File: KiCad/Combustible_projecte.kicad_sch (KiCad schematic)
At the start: 0 parts

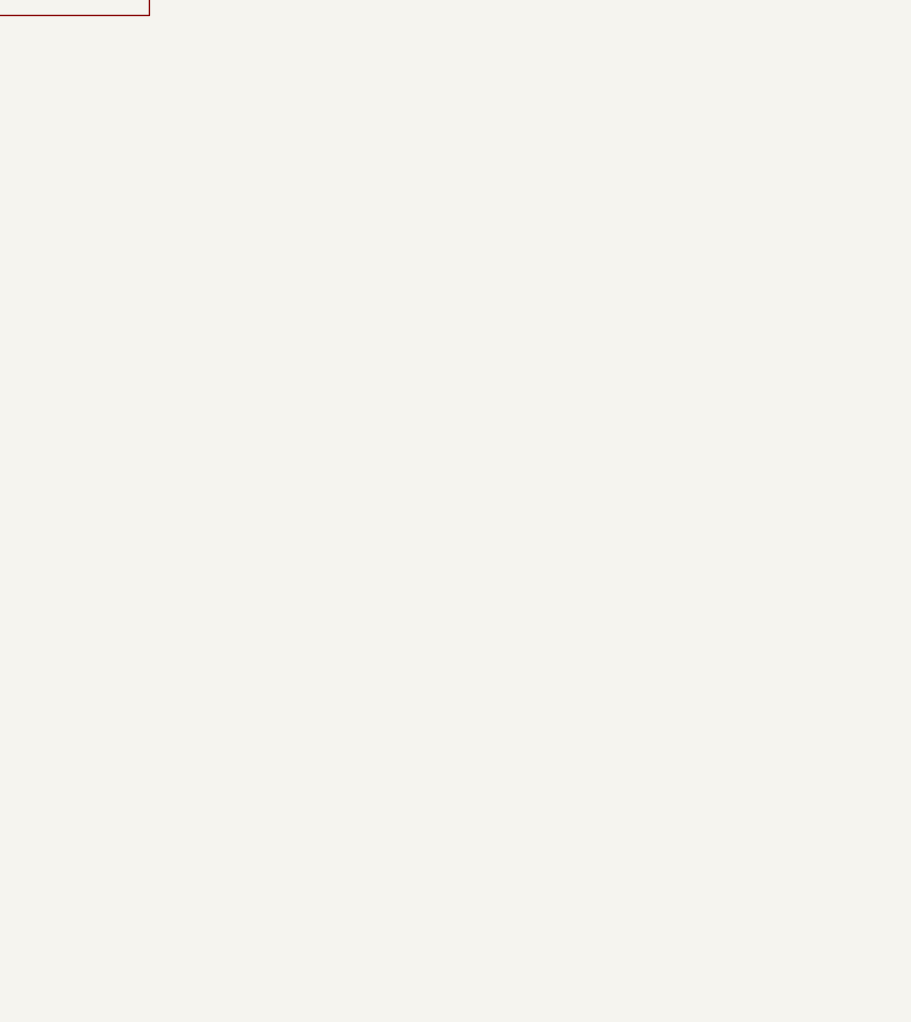
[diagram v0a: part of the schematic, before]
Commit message: Part de potencia acabada, concretar certs pins del micro
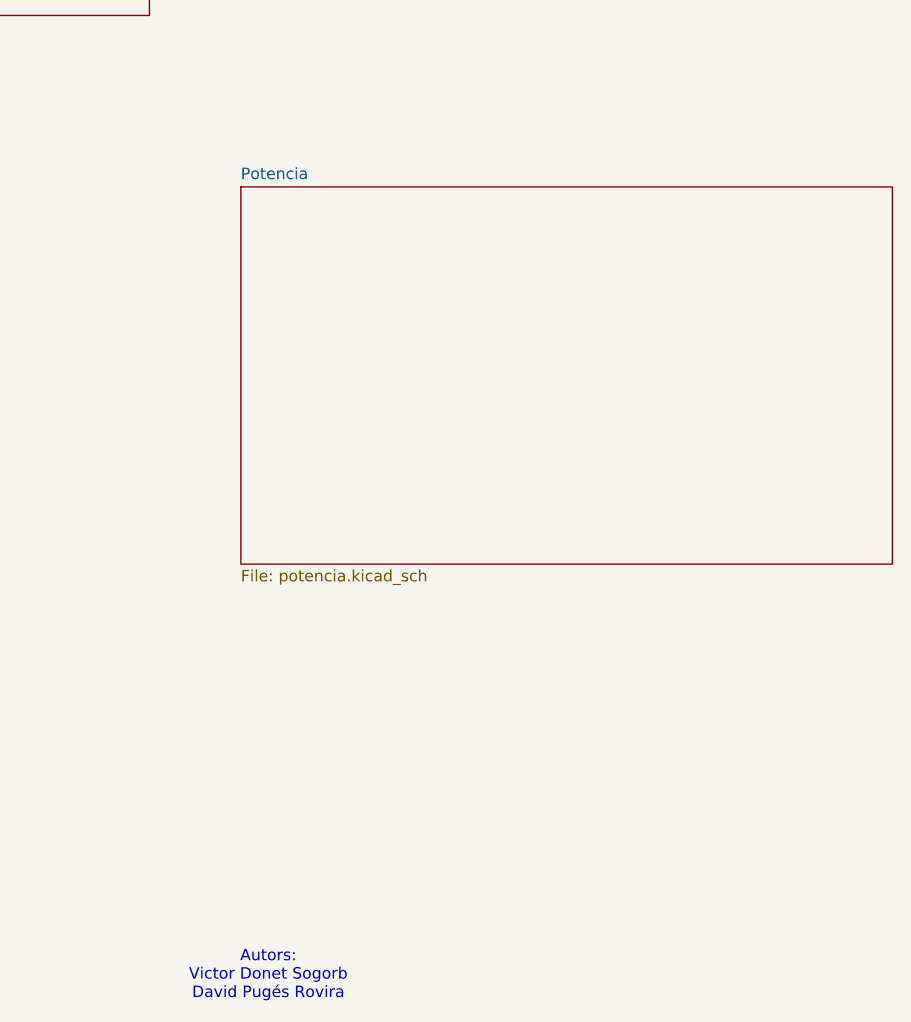
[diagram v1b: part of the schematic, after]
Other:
- added sheet Potencia (potencia.kicad_sch)
- note added: "Autors: Victor Donet Sogorb David Pugés Rovira"
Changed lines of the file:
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@@
 	(generator_version "9.0")
 	(paper "A4")
+	(text "Autors:\nVictor Donet Sogorb\nDavid Pugés Rovira"
+		(exclude_from_sim no)
+		(at 191.008 171.45 0)
+		(effects
+			(font
+				(size 1.27 1.27)
+			)
+		)
+	)
 	(sheet
 		(at 25.4 26.67)
@@
 				)
 			)
+		)
+	)
+	(sheet
+		(at 187.96 83.82)
+		(size 72.39 41.91)
+		(exclude_from_sim no)
+		(in_bom yes)
+		(on_board yes)
+		(dnp no)
+		(fields_autoplaced yes)
+		(stroke
+			(width 0.1524)
+			(type solid)
+		)
+		(fill
+			(color 0 0 0 0.0000)
+		)
+		(property "Sheetname" "Potencia"
+			(at 187.96 83.1084 0)
+			(effects
+				(font
+					(size 1.27 1.27)
+				)
+				(justify left bottom)
+			)
+		)
+		(property "Sheetfile" "potencia.kicad_sch"
+			(at 187.96 126.3146 0)
+			(effects
+				(font
+					(size 1.27 1.27)
+				)
+				(justify left top)
+			)
+		)
+		(instances
+			(project "Combustible_projecte"
+				(path "/c989196d-f442-462e-ad13-2ff17993bc1b"
+					(page "4")
+				)
+			)
